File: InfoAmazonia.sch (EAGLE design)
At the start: 21 parts, among them IC1 CA3140AM Z, IC2 TL081BCDG4, J1 BNCPTH, U1 ARDUINO-MEGAPRO

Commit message: - Placa criada
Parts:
- added C11, C12, C14, C19, C20, C21: 100nF, InfoAmazonia:C-EUC0603
- added C13, C15, C18: 10uF, InfoAmazonia:C-EUC0603
- added C16, C17: (no value), InfoAmazonia:CPOL-EUD
- added C22, C23, C24, C25, C26: 220uF, InfoAmazonia:CPOL-EUUD6,3-5,8
- added IC3: AMPOP_2R, InfoAmazonia:AMPOP_2R
- added IC4: LM2662, InfoAmazonia:LM2662
- added IC5: ADAFRUIT_FONA, InfoAmazonia:ADAFRUIT_FONA
- added IC6: SHT20, InfoAmazonia:SHT2X
- added IC7: MIC29302AWD, InfoAmazonia:MIC29XXX
- added J2: BNCPTH, InfoAmazonia:BNCPTH
- added R10, R9: 30k, InfoAmazonia:R-EU_R0603
- added R11: 75k, InfoAmazonia:R-EU_R0603
- added R12: 43k, InfoAmazonia:R-EU_R0603
- added R8: 100k, InfoAmazonia:R-EU_R0603
- added U2: MPL3115A2, InfoAmazonia:MPL3115A2LGA8
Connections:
- net N$7 renamed PH_SENSOR
- new net +VBAT: C24.+, C25.+, C26.+, IC7.OUT, R8.1
- new net N$10: C6.2
- new net N$11: C6.1
- new net N$12: C5.1
- new net N$13: IC3A.IN+, J2.OUT
- new net N$14: C16.-, IC4.CAP-
- new net N$15: C12.1, IC3A.IN-, IC3A.OUT, R10.2
- new net N$16: C16.+, IC4.CAP+
- new net N$17: IC3B.IN-, R10.1, R11.1, R9.1
- new net N$18: IC7.ADJ, R12.2, R8.2
- new net N$7: C20.1, U2.CAP
- new net N$9: C5.2
- new net OPR_SENSOR: IC3B.OUT, R9.2
- net +3V3: now also C18.1, C19.1, C21.1, IC6.VCC, U2.VDD, U2.VDDIO
- net +5V: now also C11.1, C13.1, C22.+, C23.+, IC3P.V+, IC4.V+, IC7.IN
- net -5V: now also C14.1, C15.1, C17.-, IC3P.V-, IC4.OUT, R11.2; no longer C5.1, C6.1
- net GND: now also C11.2, C12.2, C13.2, C14.2, C15.2, C17.+, C18.2, C19.2, C20.2, C21.2, C22.-, C23.-, C24.-, C25.-, C26.-, IC3B.IN+, IC4.GND, IC4.LV, IC6.GND, IC7.GND, J2.GND, R12.1, U2.GND; no longer C5.2, C6.2
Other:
- note added: "GERADOR -5V"
- note added: "PRESÃO / TEMP"
- note added: "SENSOR OPR"
- note added: "SENSOR PH"
- note added: "UMIDADE / TEMP"
- moved on the sheet: C1, C10, C2, C3, C4, C5, C6, C7, C8, C9, IC1, IC2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

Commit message: -Acho que não adicionou praticamente nada
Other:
- note added: "GERADOR +BAT"
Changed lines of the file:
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@@
 <wire x1="243.84" y1="-66.04" x2="243.84" y2="-30.48" width="0.1524" layer="94"/>
 <wire x1="243.84" y1="-30.48" x2="187.96" y2="-30.48" width="0.1524" layer="94"/>
+<text x="203.2" y="167.64" size="3.81" layer="94" ratio="10">GERADOR +BAT</text>
 </plain>
 <instances>

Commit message: [INFOA-19]
- Alguns valores de componentes alterados, bom mandado pra avaliação
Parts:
- removed C16, C17: (no value), InfoAmazonia:CPOL-EUD
- added C27, C28: 47uF, InfoAmazonia:CPOL-EUSMC_B
- IC3: value AMPOP_2R -> TL032C
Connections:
- net -5V: now also C28.-; no longer C17.-
- net GND: now also C28.+; no longer C17.+
- net N$14: now also C27.-; no longer C16.-
- net N$16: now also C27.+; no longer C16.+
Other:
- note added: "SENSOR ORP"
- note removed: "SENSOR OPR"
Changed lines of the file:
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@@
 <part name="GND11" library="InfoAmazonia" deviceset="GND" device=""/>
 <part name="J2" library="InfoAmazonia" deviceset="BNC" device="PTH"/>
-<part name="IC3" library="InfoAmazonia" deviceset="AMPOP_2" device="R"/>
+<part name="IC3" library="InfoAmazonia" deviceset="AMPOP_2" device="R" value="TL032C"/>
 <part name="GND8" library="InfoAmazonia" deviceset="GND" device=""/>
 <part name="C11" library="InfoAmazonia" deviceset="C-EU" device="C0603" value="100nF"/>
@@
 <part name="IC4" library="InfoAmazonia" deviceset="LM2662" device=""/>
 <part name="GND12" library="InfoAmazonia" deviceset="GND" device=""/>
-<part name="C16" library="InfoAmazonia" deviceset="CPOL-EU" device="D"/>
-<part name="C17" library="InfoAmazonia" deviceset="CPOL-EU" device="D"/>
 <part name="GND13" library="InfoAmazonia" deviceset="GND" device=""/>
 <part name="IC5" library="InfoAmazonia" deviceset="ADAFRUIT_FONA" device=""/>
@@
 <part name="GND21" library="InfoAmazonia" deviceset="GND" device=""/>
 <part name="GND22" library="InfoAmazonia" deviceset="GND" device=""/>
+<part name="C27" library="InfoAmazonia" deviceset="CPOL-EU" device="SMC_B" value="47uF"/>
+<part name="C28" library="InfoAmazonia" deviceset="CPOL-EU" device="SMC_B" value="47uF"/>
 </parts>
 <sheets>
@@
 <wire x1="241.3" y1="43.18" x2="241.3" y2="96.52" width="0.1524" layer="94"/>
 <wire x1="241.3" y1="96.52" x2="116.84" y2="96.52" width="0.1524" layer="94"/>
-<text x="162.56" y="91.44" size="3.81" layer="94" ratio="10">SENSOR OPR</text>
+<text x="162.56" y="91.44" size="3.81" layer="94" ratio="10">SENSOR ORP</text>
 <text x="165.1" y="33.02" size="3.81" layer="94" ratio="10">SENSOR PH</text>
 <text x="129.54" y="-35.56" size="3.81" layer="94" ratio="10">PRESÃO / TEMP</text>
@@
 </instance>
 <instance part="GND12" gate="1" x="162.56" y="144.78"/>
-<instance part="C16" gate="G$1" x="127" y="154.94" smashed="yes">
-<attribute name="NAME" x="120.523" y="155.4226" size="1.778" layer="95"/>
-<attribute name="VALUE" x="128.143" y="150.3426" size="1.778" layer="96"/>
-</instance>
-<instance part="C17" gate="G$1" x="170.18" y="149.86" smashed="yes" rot="R180">
-<attribute name="NAME" x="169.037" y="149.3774" size="1.778" layer="95" rot="R180"/>
-<attribute name="VALUE" x="169.037" y="154.4574" size="1.778" layer="96" rot="R180"/>
-</instance>
 <instance part="GND13" gate="1" x="170.18" y="144.78"/>
 <instance part="IC5" gate="G$1" x="25.4" y="109.22" rot="MR0"/>
@@
 <instance part="GND21" gate="1" x="246.38" y="142.24"/>
 <instance part="GND22" gate="1" x="254" y="142.24"/>
+<instance part="C27" gate="G$1" x="127" y="154.94"/>
+<instance part="C28" gate="G$1" x="170.18" y="149.86" rot="R180"/>
 </instances>
 <busses>
@@
 </segment>
 <segment>
-<pinref part="C17" gate="G$1" pin="+"/>
-<pinref part="GND13" gate="1" pin="GND"/>
-</segment>
-<segment>
 <wire x1="144.78" y1="-55.88" x2="142.24" y2="-55.88" width="0.1524" layer="91"/>
 <wire x1="142.24" y1="-55.88" x2="142.24" y2="-58.42" width="0.1524" layer="91"/>
@@
 <pinref part="GND22" gate="1" pin="GND"/>
 <wire x1="254" y1="147.32" x2="254" y2="144.78" width="0.1524" layer="91"/>
+</segment>
+<segment>
+<pinref part="GND13" gate="1" pin="GND"/>
+<pinref part="C28" gate="G$1" pin="+"/>
 </segment>
 </net>
@@
 <wire x1="160.02" y1="152.4" x2="162.56" y2="152.4" width="0.1524" layer="91"/>
 <wire x1="162.56" y1="152.4" x2="162.56" y2="154.94" width="0.1524" layer="91"/>
-<pinref part="C17" gate="G$1" pin="-"/>
-<wire x1="162.56" y1="154.94" x2="170.18" y2="154.94" width="0.1524" layer="91"/>
 <pinref part="P-4" gate="1" pin="-5V"/>
 <wire x1="177.8" y1="152.4" x2="177.8" y2="154.94" width="0.1524" layer="91"/>
 <wire x1="177.8" y1="154.94" x2="170.18" y2="154.94" width="0.1524" layer="91"/>
+<pinref part="C28" gate="G$1" pin="-"/>
+<wire x1="170.18" y1="154.94" x2="162.56" y2="154.94" width="0.1524" layer="91"/>
 <junction x="170.18" y="154.94"/>
 </segment>
@@
 <wire x1="137.16" y1="152.4" x2="132.08" y2="152.4" width="0.1524" layer="91"/>
 <wire x1="132.08" y1="152.4" x2="132.08" y2="149.86" width="0.1524" layer="91"/>
-<pinref part="C16" gate="G$1" pin="-"/>
 <wire x1="132.08" y1="149.86" x2="127" y2="149.86" width="0.1524" layer="91"/>
+<pinref part="C27" gate="G$1" pin="-"/>
 </segment>
 </net>
@@
 <wire x1="137.16" y1="154.94" x2="132.08" y2="154.94" width="0.1524" layer="91"/>
 <wire x1="132.08" y1="154.94" x2="132.08" y2="157.48" width="0.1524" layer="91"/>
-<pinref part="C16" gate="G$1" pin="+"/>
 <wire x1="132.08" y1="157.48" x2="127" y2="157.48" width="0.1524" layer="91"/>
-</segment>
-</net>
+<pinref part="C27" gate="G$1" pin="+"/>
+</segment>
+</net>

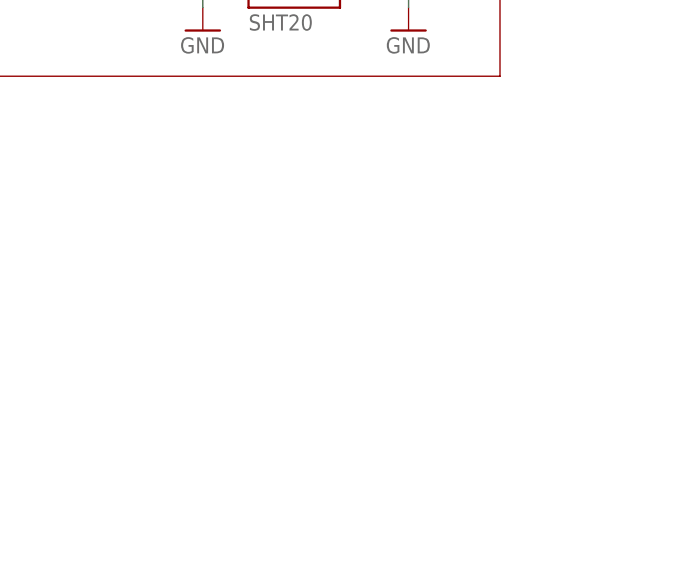
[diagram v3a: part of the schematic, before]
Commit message: - SD adicionado
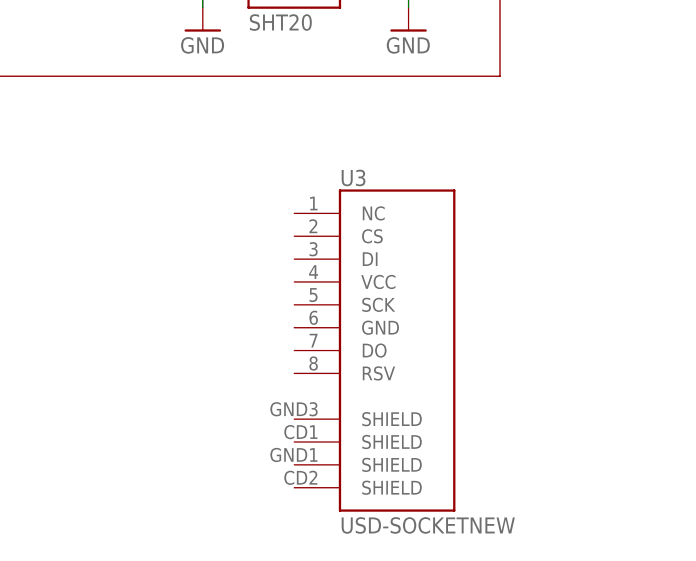
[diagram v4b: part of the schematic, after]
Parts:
- added U3: USD-SOCKETNEW, InfoAmazonia:USD-SOCKETNEW
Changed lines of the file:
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@@
 <part name="C27" library="InfoAmazonia" deviceset="CPOL-EU" device="SMC_B" value="47uF"/>
 <part name="C28" library="InfoAmazonia" deviceset="CPOL-EU" device="SMC_B" value="47uF"/>
+<part name="U3" library="InfoAmazonia" deviceset="USD-SOCKET" device="NEW"/>
 </parts>
 <sheets>
@@
 <instance part="C27" gate="G$1" x="127" y="154.94"/>
 <instance part="C28" gate="G$1" x="170.18" y="149.86" rot="R180"/>
+<instance part="U3" gate="G$1" x="228.6" y="-93.98"/>
 </instances>
 <busses>

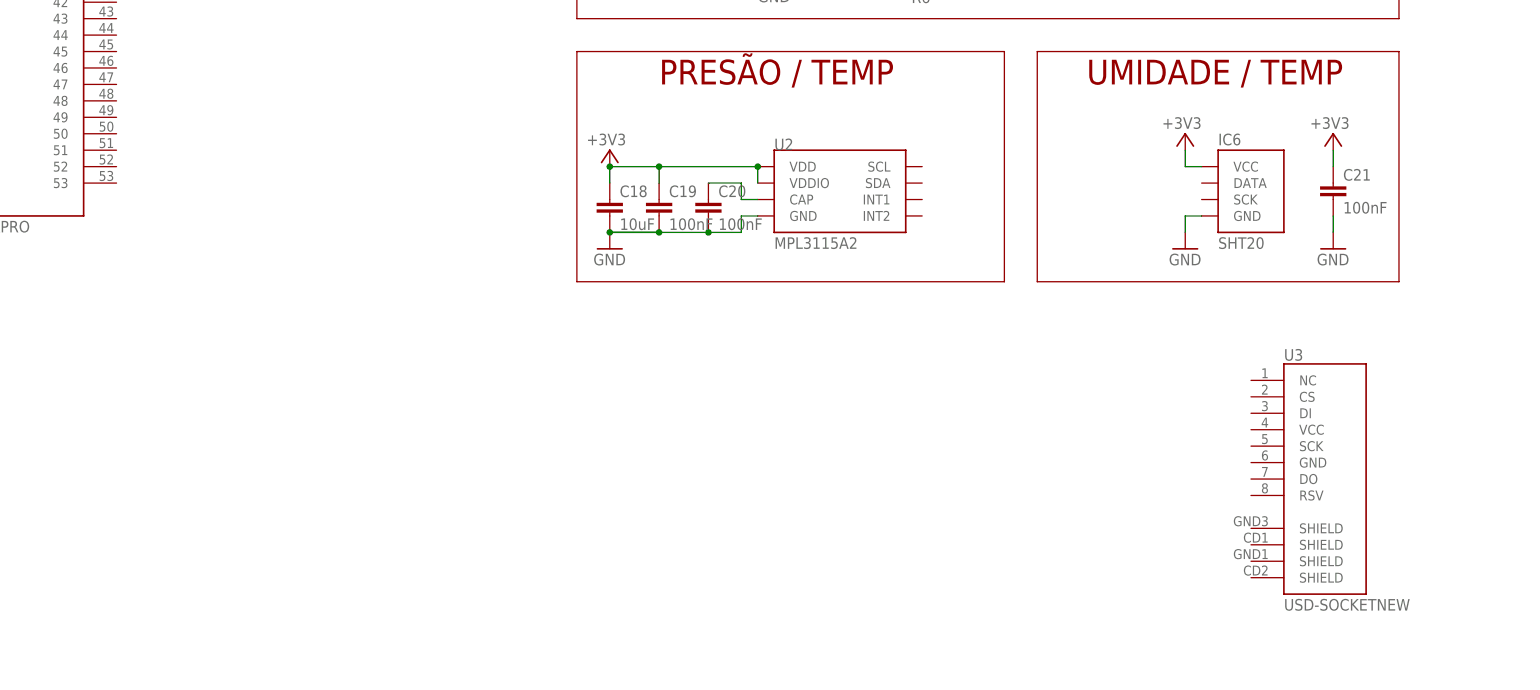
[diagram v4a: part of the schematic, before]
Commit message: - SD adicionado
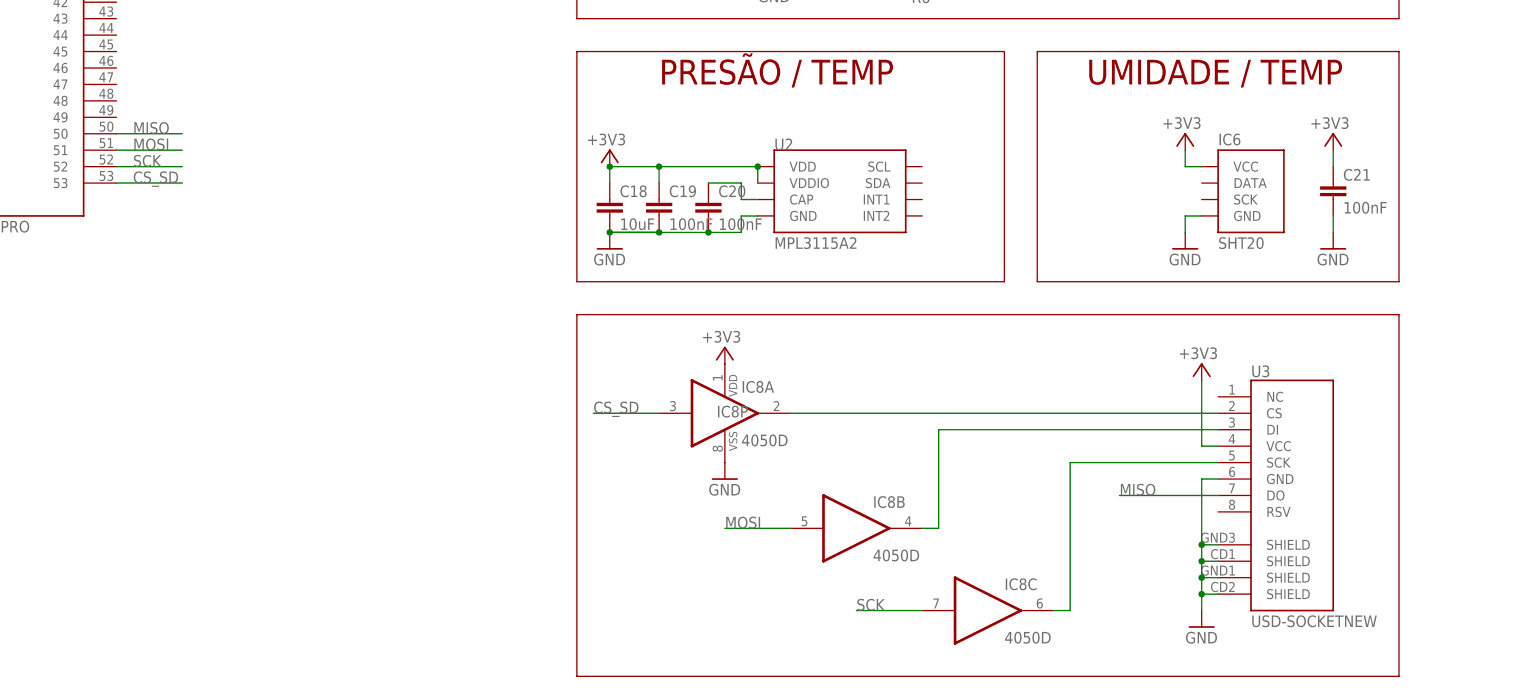
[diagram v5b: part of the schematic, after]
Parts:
- added IC8: 4050D, InfoAmazonia:4050D
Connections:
- new net CS_SD: IC8A.I, U1.53
- new net MISO: U1.50, U3.DO
- new net MOSI: IC8B.I, U1.51
- new net N$19: IC8C.O, U3.SCK
- new net N$20: IC8B.O, U3.DI
- new net N$21: IC8A.O, U3.CS
- new net SCK: IC8C.I, U1.52
- net +3V3: now also IC8P.VDD, U3.VCC
- net GND: now also IC8P.VSS, U3.GND, U3.SHIELD@1, U3.SHIELD@2, U3.SHIELD@3, U3.SHIELD@4
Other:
- moved on the sheet: U3
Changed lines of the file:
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@@
 <part name="C28" library="InfoAmazonia" deviceset="CPOL-EU" device="SMC_B" value="47uF"/>
 <part name="U3" library="InfoAmazonia" deviceset="USD-SOCKET" device="NEW"/>
+<part name="+3V6" library="InfoAmazonia" deviceset="+3V3" device=""/>
+<part name="GND24" library="InfoAmazonia" deviceset="GND" device=""/>
+<part name="IC8" library="InfoAmazonia" deviceset="4050" device="D"/>
+<part name="+3V5" library="InfoAmazonia" deviceset="+3V3" device=""/>
+<part name="GND23" library="InfoAmazonia" deviceset="GND" device=""/>
 </parts>
 <sheets>
@@
 <wire x1="243.84" y1="-30.48" x2="187.96" y2="-30.48" width="0.1524" layer="94"/>
 <text x="203.2" y="167.64" size="3.81" layer="94" ratio="10">GERADOR +BAT</text>
+<wire x1="116.84" y1="-71.12" x2="116.84" y2="-127" width="0.1524" layer="94"/>
+<wire x1="116.84" y1="-71.12" x2="243.84" y2="-71.12" width="0.1524" layer="94"/>
+<wire x1="243.84" y1="-71.12" x2="243.84" y2="-127" width="0.1524" layer="94"/>
+<wire x1="243.84" y1="-127" x2="116.84" y2="-127" width="0.1524" layer="94"/>
 </plain>
 <instances>
@@
 <instance part="C27" gate="G$1" x="127" y="154.94"/>
 <instance part="C28" gate="G$1" x="170.18" y="149.86" rot="R180"/>
-<instance part="U3" gate="G$1" x="228.6" y="-93.98"/>
+<instance part="U3" gate="G$1" x="223.52" y="-96.52"/>
+<instance part="+3V6" gate="G$1" x="213.36" y="-78.74" smashed="yes">
+<attribute name="VALUE" x="215.9" y="-76.2" size="1.778" layer="96" rot="R180"/>
+</instance>
+<instance part="GND24" gate="1" x="213.36" y="-119.38"/>
+<instance part="IC8" gate="A" x="139.7" y="-86.36"/>
+<instance part="IC8" gate="B" x="160.02" y="-104.14"/>
+<instance part="IC8" gate="C" x="180.34" y="-116.84"/>
+<instance part="IC8" gate="P" x="139.7" y="-86.36"/>
+<instance part="+3V5" gate="G$1" x="139.7" y="-76.2" smashed="yes">
+<attribute name="VALUE" x="142.24" y="-73.66" size="1.778" layer="96" rot="R180"/>
+</instance>
+<instance part="GND23" gate="1" x="139.7" y="-96.52"/>
 </instances>
 <busses>
@@
 <pinref part="C28" gate="G$1" pin="+"/>
 </segment>
+<segment>
+<pinref part="U3" gate="G$1" pin="GND"/>
+<pinref part="GND24" gate="1" pin="GND"/>
+<wire x1="215.9" y1="-96.52" x2="213.36" y2="-96.52" width="0.1524" layer="91"/>
+<wire x1="213.36" y1="-96.52" x2="213.36" y2="-106.68" width="0.1524" layer="91"/>
+<junction x="213.36" y="-106.68"/>
+<wire x1="213.36" y1="-106.68" x2="213.36" y2="-109.22" width="0.1524" layer="91"/>
+<junction x="213.36" y="-109.22"/>
+<wire x1="213.36" y1="-109.22" x2="213.36" y2="-111.76" width="0.1524" layer="91"/>
+<junction x="213.36" y="-111.76"/>
+<wire x1="213.36" y1="-111.76" x2="213.36" y2="-114.3" width="0.1524" layer="91"/>
+<junction x="213.36" y="-114.3"/>
+<wire x1="213.36" y1="-114.3" x2="213.36" y2="-116.84" width="0.1524" layer="91"/>
+<pinref part="U3" gate="G$1" pin="SHIELD@4"/>
+<wire x1="215.9" y1="-114.3" x2="213.36" y2="-114.3" width="0.1524" layer="91"/>
+<pinref part="U3" gate="G$1" pin="SHIELD@3"/>
+<wire x1="215.9" y1="-111.76" x2="213.36" y2="-111.76" width="0.1524" layer="91"/>
+<pinref part="U3" gate="G$1" pin="SHIELD@2"/>
+<wire x1="215.9" y1="-109.22" x2="213.36" y2="-109.22" width="0.1524" layer="91"/>
+<pinref part="U3" gate="G$1" pin="SHIELD@1"/>
+<wire x1="215.9" y1="-106.68" x2="213.36" y2="-106.68" width="0.1524" layer="91"/>
+</segment>
+<segment>
+<pinref part="IC8" gate="P" pin="VSS"/>
+<pinref part="GND23" gate="1" pin="GND"/>
+</segment>
 </net>
 <net name="+5V" class="0">
@@
 <pinref part="+3V4" gate="G$1" pin="+3V3"/>
 <wire x1="233.68" y1="-45.72" x2="233.68" y2="-48.26" width="0.1524" layer="91"/>
+</segment>
+<segment>
+<pinref part="U3" gate="G$1" pin="VCC"/>
+<pinref part="+3V6" gate="G$1" pin="+3V3"/>
+<wire x1="215.9" y1="-91.44" x2="213.36" y2="-91.44" width="0.1524" layer="91"/>
+<wire x1="213.36" y1="-91.44" x2="213.36" y2="-81.28" width="0.1524" layer="91"/>
+</segment>
+<segment>
+<pinref part="IC8" gate="P" pin="VDD"/>
+<pinref part="+3V5" gate="G$1" pin="+3V3"/>
 </segment>
 </net>
@@
 </segment>
 </net>
+<net name="MOSI" class="0">
+<segment>
+<wire x1="149.86" y1="-104.14" x2="139.7" y2="-104.14" width="0.1524" layer="91"/>
+<pinref part="IC8" gate="B" pin="I"/>
+<label x="139.7" y="-104.14" size="1.778" layer="95"/>
+</segment>
+<segment>
+<pinref part="U1" gate="G$1" pin="51"/>
+<wire x1="45.72" y1="-45.72" x2="55.88" y2="-45.72" width="0.1524" layer="91"/>
+<label x="48.26" y="-45.72" size="1.778" layer="95"/>
+</segment>
+</net>
+<net name="MISO" class="0">
+<segment>
+<wire x1="215.9" y1="-99.06" x2="200.66" y2="-99.06" width="0.1524" layer="91"/>
+<label x="200.66" y="-99.06" size="1.778" layer="95"/>
+<pinref part="U3" gate="G$1" pin="DO"/>
+</segment>
+<segment>
+<pinref part="U1" gate="G$1" pin="50"/>
+<wire x1="45.72" y1="-43.18" x2="55.88" y2="-43.18" width="0.1524" layer="91"/>
+<label x="48.26" y="-43.18" size="1.778" layer="95"/>
+</segment>
+</net>
+<net name="CS_SD" class="0">
+<segment>
+<pinref part="IC8" gate="A" pin="I"/>
+<wire x1="129.54" y1="-86.36" x2="119.38" y2="-86.36" width="0.1524" layer="91"/>
+<label x="119.38" y="-86.36" size="1.778" layer="95"/>
+</segment>
+<segment>
+<pinref part="U1" gate="G$1" pin="53"/>
+<wire x1="45.72" y1="-50.8" x2="55.88" y2="-50.8" width="0.1524" layer="91"/>
+<label x="48.26" y="-50.8" size="1.778" layer="95"/>
+</segment>
+</net>
+<net name="N$19" class="0">
+<segment>
+<pinref part="U3" gate="G$1" pin="SCK"/>
+<wire x1="215.9" y1="-93.98" x2="193.04" y2="-93.98" width="0.1524" layer="91"/>
+<wire x1="193.04" y1="-93.98" x2="193.04" y2="-116.84" width="0.1524" layer="91"/>
+<pinref part="IC8" gate="C" pin="O"/>
+<wire x1="193.04" y1="-116.84" x2="190.5" y2="-116.84" width="0.1524" layer="91"/>
+</segment>
+</net>
+<net name="SCK" class="0">
+<segment>
+<wire x1="170.18" y1="-116.84" x2="160.02" y2="-116.84" width="0.1524" layer="91"/>
+<label x="160.02" y="-116.84" size="1.778" layer="95"/>
+<pinref part="IC8" gate="C" pin="I"/>
+</segment>
+<segment>
+<pinref part="U1" gate="G$1" pin="52"/>
+<wire x1="45.72" y1="-48.26" x2="55.88" y2="-48.26" width="0.1524" layer="91"/>
+<label x="48.26" y="-48.26" size="1.778" layer="95"/>
+</segment>
+</net>
+<net name="N$20" class="0">
+<segment>
+<pinref part="U3" gate="G$1" pin="DI"/>
+<wire x1="215.9" y1="-88.9" x2="172.72" y2="-88.9" width="0.1524" layer="91"/>
+<wire x1="172.72" y1="-88.9" x2="172.72" y2="-104.14" width="0.1524" layer="91"/>
+<pinref part="IC8" gate="B" pin="O"/>
+<wire x1="172.72" y1="-104.14" x2="170.18" y2="-104.14" width="0.1524" layer="91"/>
+</segment>
+</net>
+<net name="N$21" class="0">
+<segment>
+<pinref part="U3" gate="G$1" pin="CS"/>
+<pinref part="IC8" gate="A" pin="O"/>
+<wire x1="215.9" y1="-86.36" x2="149.86" y2="-86.36" width="0.1524" layer="91"/>
+</segment>
+</net>
